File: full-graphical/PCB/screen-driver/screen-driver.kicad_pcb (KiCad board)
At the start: 2 copper layers, 139 x 139 mm, 159 parts, among them J1 Barrel_Jack_Switch, Q1 MPSA42, Q10 MPSA42, Q11 MPSA42, Q12 MPSA42, Q13 MPSA42, Q14 MPSA42, Q15 MPSA42, Q16 MPSA42, Q17 MPSA42, Q18 MPSA42, Q19 MPSA42, Q2 MPSA42, Q20 MPSA42, Q21 MPSA42, Q22 MPSA42, Q23 MPSA42, Q24 MPSA42, Q25 MPSA42, Q26 MPSA42, Q27 MPSA42, Q28 MPSA42, Q29 MPSA42, Q3 MPSA42, Q30 MPSA42, Q31 MPSA42, Q32 MPSA42, Q4 MPSA42, Q5 MPSA42, Q6 MPSA42, Q7 MPSA42, Q8 MPSA42, Q9 MPSA42, U1 SN755870, U2 ESP32-DEVKIT-V1, U3 SN755870, U4 TSR_1-2450, U5 CD4017BE, U6 CD4017BE

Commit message: first draft of full pcb
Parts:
- removed R117, R118, R119, R120, R121, R122, R123, R124, R125, R126: R, Resistor_THT:R_Axial_DIN0207_L6.3mm_D2.5mm_P7.62mm_Horizontal
- added C1: C_Small, Capacitor_THT:C_Disc_D3.8mm_W2.6mm_P2.50mm, F.Cu at (164.8, 72.6)
- added C2: C_Small, Capacitor_THT:C_Disc_D3.8mm_W2.6mm_P2.50mm, F.Cu at (212.3, 91.9)
- added C3: C_Small, Capacitor_THT:C_Disc_D3.8mm_W2.6mm_P2.50mm, F.Cu at (193.9, 63.3)
- added C4: C_Small, Capacitor_THT:C_Disc_D3.8mm_W2.6mm_P2.50mm, F.Cu at (145.6, 88.3)
- added J10: Conn_01x05_Male, Connector_PinHeader_2.54mm:PinHeader_1x05_P2.54mm_Vertical, B.Cu at (158.2, 83.3)
- added J2: ANODE - EVEN 2-60, Connector_PinHeader_2.00mm:PinHeader_1x40_P2.00mm_Vertical, F.Cu at (91.3, 33.2)
- added J3: ANODE - EVEN-62-100, Connector_PinHeader_2.00mm:PinHeader_1x20_P2.00mm_Vertical, F.Cu at (91.3, 113.2)
- added J4: CATHODE - EVEN - 42-100, Connector_PinHeader_2.00mm:PinHeader_1x40_P2.00mm_Vertical, F.Cu at (104.9, 28.1)
- added J5: CATHODE ODD 41-99, Connector_PinHeader_2.00mm:PinHeader_1x40_P2.00mm_Vertical, F.Cu at (104.7, 157.2)
- added J6: CATHODE EVEN 2-40, Connector_PinHeader_2.00mm:PinHeader_1x12_P2.00mm_Vertical, F.Cu at (184.9, 28.1)
- added J7: CATHODE ODD 1-39, Connector_PinHeader_2.00mm:PinHeader_1x12_P2.00mm_Vertical, F.Cu at (184.7, 157.2)
- added J8: ANODE - ODD 1-59, Connector_PinHeader_2.00mm:PinHeader_1x40_P2.00mm_Vertical, F.Cu at (220.3, 33.2)
- added J9: ANODE - ODD 61-99, Connector_PinHeader_2.00mm:PinHeader_1x20_P2.00mm_Vertical, F.Cu at (220.3, 113.2)
- added R111: R, Resistor_SMD:R_0201_0603Metric_Pad0.64x0.40mm_HandSolder, F.Cu at (217.0, 143.2)
- added R112: R, Resistor_THT:R_Axial_DIN0207_L6.3mm_D2.5mm_P7.62mm_Horizontal, F.Cu at (186.4, 45.8)
- added R113: R, Resistor_THT:R_Axial_DIN0207_L6.3mm_D2.5mm_P7.62mm_Horizontal, F.Cu at (158.4, 88.4)
- J1, U4: moved to B.Cu
- R102, R103, R104, R105, R106, R107, R108, R109, R110: footprint Resistor_THT:R_Axial_DIN0207_L6.3mm_D2.5mm_P7.62mm_Horizontal -> Resistor_SMD:R_0201_0603Metric_Pad0.64x0.40mm_HandSolder
- R51, R52, R53, R54, R55, R56, R57, R58, R59, R60: footprint Resistor_SMD:R_0201_0603Metric_Pad0.64x0.40mm_HandSolder -> Resistor_THT:R_Axial_DIN0207_L6.3mm_D2.5mm_P7.62mm_Horizontal
- U2: footprint ESP32-DEVKIT-V1:MODULE_ESP32_DEVKIT_V1 -> ESP32-DEVKITC-32D:MODULE_ESP32-DEVKITC-32D; moved to B.Cu
- U5, U6: footprint CD4017BE:DIP794W45P254L1969H508Q16 -> Package_DIP:DIP-16_W7.62mm
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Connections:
- J1 pad 1: unconnected-(J1-Pad1) -> Net-(J1-Pad1)
- J1 pad 2: unconnected-(J1-Pad2) -> GND
- Q1 pad 1: unconnected-(Q1-Pad1) -> GND
- Q1 pad 2: unconnected-(Q1-Pad2) -> Net-(Q1-Pad2)
- Q1 pad 3: unconnected-(Q1-Pad3) -> Net-(J3-Pad20)
- Q10 pad 1: unconnected-(Q10-Pad1) -> GND
- Q10 pad 2: unconnected-(Q10-Pad2) -> Net-(Q10-Pad2)
- Q10 pad 3: unconnected-(Q10-Pad3) -> Net-(J3-Pad17)
- Q11 pad 1: unconnected-(Q11-Pad1) -> Net-(Q11-Pad1)
- Q11 pad 2: unconnected-(Q11-Pad2) -> Net-(Q1-Pad2)
- Q11 pad 3: unconnected-(Q11-Pad3) -> Net-(J7-Pad11)
- Q12 pad 1: unconnected-(Q12-Pad1) -> Net-(Q11-Pad1)
- Q12 pad 2: unconnected-(Q12-Pad2) -> Net-(Q12-Pad2)
- Q12 pad 3: unconnected-(Q12-Pad3) -> Net-(J6-Pad11)
- Q13 pad 1: unconnected-(Q13-Pad1) -> Net-(Q11-Pad1)
- Q13 pad 2: unconnected-(Q13-Pad2) -> Net-(Q13-Pad2)
- Q13 pad 3: unconnected-(Q13-Pad3) -> Net-(J6-Pad8)
- Q14 pad 1: unconnected-(Q14-Pad1) -> Net-(Q11-Pad1)
- Q14 pad 2: unconnected-(Q14-Pad2) -> Net-(Q14-Pad2)
- Q14 pad 3: unconnected-(Q14-Pad3) -> Net-(J6-Pad5)
- Q15 pad 1: unconnected-(Q15-Pad1) -> Net-(Q11-Pad1)
- Q15 pad 2: unconnected-(Q15-Pad2) -> Net-(Q15-Pad2)
- Q15 pad 3: unconnected-(Q15-Pad3) -> Net-(J6-Pad2)
- Q16 pad 1: unconnected-(Q16-Pad1) -> Net-(Q11-Pad1)
- Q16 pad 2: unconnected-(Q16-Pad2) -> Net-(Q10-Pad2)
- Q16 pad 3: unconnected-(Q16-Pad3) -> Net-(J4-Pad39)
- Q17 pad 1: unconnected-(Q17-Pad1) -> Net-(Q11-Pad1)
- Q17 pad 2: unconnected-(Q17-Pad2) -> Net-(Q17-Pad2)
- Q17 pad 3: unconnected-(Q17-Pad3) -> Net-(J4-Pad36)
- Q18 pad 1: unconnected-(Q18-Pad1) -> Net-(Q11-Pad1)
- Q18 pad 2: unconnected-(Q18-Pad2) -> Net-(Q18-Pad2)
- Q18 pad 3: unconnected-(Q18-Pad3) -> Net-(J4-Pad33)
- Q19 pad 1: unconnected-(Q19-Pad1) -> Net-(Q11-Pad1)
- Q19 pad 2: unconnected-(Q19-Pad2) -> Net-(Q19-Pad2)
- Q19 pad 3: unconnected-(Q19-Pad3) -> Net-(J4-Pad30)
- Q2 pad 1: unconnected-(Q2-Pad1) -> GND
- Q2 pad 2: unconnected-(Q2-Pad2) -> Net-(Q12-Pad2)
- Q2 pad 3: unconnected-(Q2-Pad3) -> Net-(J2-Pad4)
- Q20 pad 1: unconnected-(Q20-Pad1) -> Net-(Q11-Pad1)
- Q20 pad 2: unconnected-(Q20-Pad2) -> Net-(Q20-Pad2)
- Q20 pad 3: unconnected-(Q20-Pad3) -> Net-(J4-Pad27)
- Q21 pad 1: unconnected-(Q21-Pad1) -> GND
- Q21 pad 2: unconnected-(Q21-Pad2) -> Net-(Q21-Pad2)
- Q21 pad 3: unconnected-(Q21-Pad3) -> Net-(Q11-Pad1)
- Q22 pad 1: unconnected-(Q22-Pad1) -> Net-(Q22-Pad1)
- Q22 pad 2: unconnected-(Q22-Pad2) -> Net-(Q1-Pad2)
- Q22 pad 3: unconnected-(Q22-Pad3) -> Net-(J4-Pad24)
- Q23 pad 1: unconnected-(Q23-Pad1) -> Net-(Q22-Pad1)
- Q23 pad 2: unconnected-(Q23-Pad2) -> Net-(Q12-Pad2)
- Q23 pad 3: unconnected-(Q23-Pad3) -> Net-(J4-Pad21)
- Q24 pad 1: unconnected-(Q24-Pad1) -> Net-(Q22-Pad1)
- Q24 pad 2: unconnected-(Q24-Pad2) -> Net-(Q13-Pad2)
- Q24 pad 3: unconnected-(Q24-Pad3) -> Net-(J4-Pad18)
- Q25 pad 1: unconnected-(Q25-Pad1) -> Net-(Q22-Pad1)
- Q25 pad 2: unconnected-(Q25-Pad2) -> Net-(Q14-Pad2)
- Q25 pad 3: unconnected-(Q25-Pad3) -> Net-(J4-Pad15)
- Q26 pad 1: unconnected-(Q26-Pad1) -> Net-(Q22-Pad1)
- Q26 pad 2: unconnected-(Q26-Pad2) -> Net-(Q15-Pad2)
- Q26 pad 3: unconnected-(Q26-Pad3) -> Net-(J4-Pad12)
- Q27 pad 1: unconnected-(Q27-Pad1) -> Net-(Q22-Pad1)
- Q27 pad 2: unconnected-(Q27-Pad2) -> Net-(Q10-Pad2)
- Q27 pad 3: unconnected-(Q27-Pad3) -> Net-(J4-Pad9)
- Q28 pad 1: unconnected-(Q28-Pad1) -> Net-(Q22-Pad1)
- Q28 pad 2: unconnected-(Q28-Pad2) -> Net-(Q17-Pad2)
- Q28 pad 3: unconnected-(Q28-Pad3) -> Net-(J4-Pad6)
- Q29 pad 1: unconnected-(Q29-Pad1) -> Net-(Q22-Pad1)
- Q29 pad 2: unconnected-(Q29-Pad2) -> Net-(Q18-Pad2)
- Q29 pad 3: unconnected-(Q29-Pad3) -> Net-(J4-Pad3)
- Q3 pad 1: unconnected-(Q3-Pad1) -> GND
- Q3 pad 2: unconnected-(Q3-Pad2) -> Net-(Q13-Pad2)
- Q3 pad 3: unconnected-(Q3-Pad3) -> Net-(J3-Pad18)
- Q30 pad 1: unconnected-(Q30-Pad1) -> Net-(Q22-Pad1)
- Q30 pad 2: unconnected-(Q30-Pad2) -> Net-(Q19-Pad2)
- Q30 pad 3: unconnected-(Q30-Pad3) -> Net-(J5-Pad1)
- Q31 pad 1: unconnected-(Q31-Pad1) -> Net-(Q22-Pad1)
- Q31 pad 2: unconnected-(Q31-Pad2) -> Net-(Q20-Pad2)
- Q31 pad 3: unconnected-(Q31-Pad3) -> Net-(J4-Pad2)
- Q32 pad 1: unconnected-(Q32-Pad1) -> GND
- Q32 pad 2: unconnected-(Q32-Pad2) -> Net-(Q32-Pad2)
- Q32 pad 3: unconnected-(Q32-Pad3) -> Net-(Q22-Pad1)
- Q4 pad 1: unconnected-(Q4-Pad1) -> GND
- Q4 pad 2: unconnected-(Q4-Pad2) -> Net-(Q20-Pad2)
- Q4 pad 3: unconnected-(Q4-Pad3) -> Net-(J2-Pad30)
- Q5 pad 1: unconnected-(Q5-Pad1) -> GND
- Q5 pad 2: unconnected-(Q5-Pad2) -> Net-(Q14-Pad2)
- Q5 pad 3: unconnected-(Q5-Pad3) -> Net-(J2-Pad1)
- Q6 pad 1: unconnected-(Q6-Pad1) -> GND
- Q6 pad 2: unconnected-(Q6-Pad2) -> Net-(Q19-Pad2)
- Q6 pad 3: unconnected-(Q6-Pad3) -> Net-(J2-Pad2)
- Q7 pad 1: unconnected-(Q7-Pad1) -> GND
- Q7 pad 2: unconnected-(Q7-Pad2) -> Net-(Q15-Pad2)
- Q7 pad 3: unconnected-(Q7-Pad3) -> Net-(J3-Pad19)
- Q8 pad 1: unconnected-(Q8-Pad1) -> GND
- Q8 pad 2: unconnected-(Q8-Pad2) -> Net-(Q18-Pad2)
- Q8 pad 3: unconnected-(Q8-Pad3) -> Net-(J2-Pad31)
- Q9 pad 1: unconnected-(Q9-Pad1) -> GND
- Q9 pad 2: unconnected-(Q9-Pad2) -> Net-(Q17-Pad2)
- Q9 pad 3: unconnected-(Q9-Pad3) -> Net-(J2-Pad3)
- R1 pad 1: unconnected-(R1-Pad1) -> Net-(J2-Pad5)
- R1 pad 2: unconnected-(R1-Pad2) -> Net-(R1-Pad2)
- R10 pad 1: unconnected-(R10-Pad1) -> Net-(J2-Pad14)
- R10 pad 2: unconnected-(R10-Pad2) -> Net-(R10-Pad2)
- R100 pad 1: unconnected-(R100-Pad1) -> Net-(J9-Pad6)
- R100 pad 2: unconnected-(R100-Pad2) -> Net-(R100-Pad2)
- R101 pad 1: unconnected-(R101-Pad1) -> Net-(R101-Pad1)
- R101 pad 2: unconnected-(R101-Pad2) -> Net-(Q20-Pad2)
- R102 pad 1: unconnected-(R102-Pad1) -> Net-(J9-Pad7)
- R102 pad 2: unconnected-(R102-Pad2) -> Net-(R102-Pad2)
- R103 pad 1: unconnected-(R103-Pad1) -> Net-(J9-Pad8)
- R103 pad 2: unconnected-(R103-Pad2) -> Net-(R103-Pad2)
- R104 pad 1: unconnected-(R104-Pad1) -> Net-(J9-Pad9)
- R104 pad 2: unconnected-(R104-Pad2) -> Net-(R104-Pad2)
- R105 pad 1: unconnected-(R105-Pad1) -> Net-(J9-Pad10)
- R105 pad 2: unconnected-(R105-Pad2) -> Net-(R105-Pad2)
- R106 pad 1: unconnected-(R106-Pad1) -> Net-(J9-Pad11)
- R106 pad 2: unconnected-(R106-Pad2) -> Net-(R106-Pad2)
- R107 pad 1: unconnected-(R107-Pad1) -> Net-(J9-Pad12)
- R107 pad 2: unconnected-(R107-Pad2) -> Net-(R107-Pad2)
- R108 pad 1: unconnected-(R108-Pad1) -> Net-(J9-Pad13)
- R108 pad 2: unconnected-(R108-Pad2) -> Net-(R108-Pad2)
- R109 pad 1: unconnected-(R109-Pad1) -> Net-(J9-Pad14)
- R109 pad 2: unconnected-(R109-Pad2) -> Net-(R109-Pad2)
- R11 pad 1: unconnected-(R11-Pad1) -> Net-(J2-Pad15)
- R11 pad 2: unconnected-(R11-Pad2) -> Net-(R11-Pad2)
- R110 pad 1: unconnected-(R110-Pad1) -> Net-(J9-Pad15)
- R110 pad 2: unconnected-(R110-Pad2) -> Net-(R110-Pad2)
- R12 pad 1: unconnected-(R12-Pad1) -> Net-(J2-Pad16)
- R12 pad 2: unconnected-(R12-Pad2) -> Net-(R12-Pad2)
- R13 pad 1: unconnected-(R13-Pad1) -> Net-(J2-Pad17)
- R13 pad 2: unconnected-(R13-Pad2) -> Net-(R13-Pad2)
- R14 pad 1: unconnected-(R14-Pad1) -> Net-(J2-Pad18)
- R14 pad 2: unconnected-(R14-Pad2) -> Net-(R14-Pad2)
- R15 pad 1: unconnected-(R15-Pad1) -> Net-(J2-Pad19)
- R15 pad 2: unconnected-(R15-Pad2) -> Net-(R15-Pad2)
- R16 pad 1: unconnected-(R16-Pad1) -> Net-(J2-Pad20)
- R16 pad 2: unconnected-(R16-Pad2) -> Net-(R16-Pad2)
- R17 pad 1: unconnected-(R17-Pad1) -> Net-(J2-Pad21)
- R17 pad 2: unconnected-(R17-Pad2) -> Net-(R17-Pad2)
- R18 pad 1: unconnected-(R18-Pad1) -> Net-(J2-Pad22)
- R18 pad 2: unconnected-(R18-Pad2) -> Net-(R18-Pad2)
- R19 pad 1: unconnected-(R19-Pad1) -> Net-(J2-Pad23)
- R19 pad 2: unconnected-(R19-Pad2) -> Net-(R19-Pad2)
- R2 pad 1: unconnected-(R2-Pad1) -> Net-(J2-Pad6)
- R2 pad 2: unconnected-(R2-Pad2) -> Net-(R2-Pad2)
- R20 pad 1: unconnected-(R20-Pad1) -> Net-(J2-Pad24)
- R20 pad 2: unconnected-(R20-Pad2) -> Net-(R20-Pad2)
- R21 pad 1: unconnected-(R21-Pad1) -> Net-(J2-Pad25)
- R21 pad 2: unconnected-(R21-Pad2) -> Net-(R21-Pad2)
- R22 pad 1: unconnected-(R22-Pad1) -> Net-(J2-Pad26)
- R22 pad 2: unconnected-(R22-Pad2) -> Net-(R22-Pad2)
- R23 pad 1: unconnected-(R23-Pad1) -> Net-(J2-Pad27)
- R23 pad 2: unconnected-(R23-Pad2) -> Net-(R23-Pad2)
- R24 pad 1: unconnected-(R24-Pad1) -> Net-(J2-Pad28)
- R24 pad 2: unconnected-(R24-Pad2) -> Net-(R24-Pad2)
- R25 pad 1: unconnected-(R25-Pad1) -> Net-(J2-Pad29)
- R25 pad 2: unconnected-(R25-Pad2) -> Net-(R25-Pad2)
- R26 pad 1: unconnected-(R26-Pad1) -> Net-(J2-Pad32)
- R26 pad 2: unconnected-(R26-Pad2) -> Net-(R26-Pad2)
- R27 pad 1: unconnected-(R27-Pad1) -> Net-(J2-Pad33)
- R27 pad 2: unconnected-(R27-Pad2) -> Net-(R27-Pad2)
- R28 pad 1: unconnected-(R28-Pad1) -> Net-(J2-Pad34)
- R28 pad 2: unconnected-(R28-Pad2) -> Net-(R28-Pad2)
- R29 pad 1: unconnected-(R29-Pad1) -> Net-(J2-Pad35)
- R29 pad 2: unconnected-(R29-Pad2) -> Net-(R29-Pad2)
- R3 pad 1: unconnected-(R3-Pad1) -> Net-(J2-Pad7)
- R3 pad 2: unconnected-(R3-Pad2) -> Net-(R3-Pad2)
- R30 pad 1: unconnected-(R30-Pad1) -> Net-(J2-Pad36)
- R30 pad 2: unconnected-(R30-Pad2) -> Net-(R30-Pad2)
- R31 pad 1: unconnected-(R31-Pad1) -> Net-(J2-Pad37)
- R31 pad 2: unconnected-(R31-Pad2) -> Net-(R31-Pad2)
- R32 pad 1: unconnected-(R32-Pad1) -> Net-(J2-Pad38)
- R32 pad 2: unconnected-(R32-Pad2) -> Net-(R32-Pad2)
- R33 pad 1: unconnected-(R33-Pad1) -> Net-(J2-Pad39)
- R33 pad 2: unconnected-(R33-Pad2) -> Net-(R33-Pad2)
- R34 pad 1: unconnected-(R34-Pad1) -> Net-(J2-Pad40)
- R34 pad 2: unconnected-(R34-Pad2) -> Net-(R34-Pad2)
- R35 pad 1: unconnected-(R35-Pad1) -> Net-(J3-Pad1)
- R35 pad 2: unconnected-(R35-Pad2) -> Net-(R35-Pad2)
- R36 pad 1: unconnected-(R36-Pad1) -> Net-(J3-Pad2)
- R36 pad 2: unconnected-(R36-Pad2) -> Net-(R36-Pad2)
- R37 pad 1: unconnected-(R37-Pad1) -> Net-(J3-Pad3)
- R37 pad 2: unconnected-(R37-Pad2) -> Net-(R37-Pad2)
- R38 pad 1: unconnected-(R38-Pad1) -> Net-(J3-Pad4)
- R38 pad 2: unconnected-(R38-Pad2) -> Net-(R38-Pad2)
- R39 pad 1: unconnected-(R39-Pad1) -> Net-(J3-Pad5)
- R39 pad 2: unconnected-(R39-Pad2) -> Net-(R39-Pad2)
- R4 pad 1: unconnected-(R4-Pad1) -> Net-(J2-Pad8)
- R4 pad 2: unconnected-(R4-Pad2) -> Net-(R4-Pad2)
- R40 pad 1: unconnected-(R40-Pad1) -> Net-(J3-Pad6)
- R40 pad 2: unconnected-(R40-Pad2) -> Net-(R40-Pad2)
- R41 pad 1: unconnected-(R41-Pad1) -> Net-(J3-Pad7)
- R41 pad 2: unconnected-(R41-Pad2) -> Net-(R41-Pad2)
- R42 pad 1: unconnected-(R42-Pad1) -> Net-(J3-Pad8)
- R42 pad 2: unconnected-(R42-Pad2) -> Net-(R42-Pad2)
- R43 pad 1: unconnected-(R43-Pad1) -> Net-(J3-Pad9)
- R43 pad 2: unconnected-(R43-Pad2) -> Net-(R43-Pad2)
- R44 pad 1: unconnected-(R44-Pad1) -> Net-(J3-Pad10)
- R44 pad 2: unconnected-(R44-Pad2) -> Net-(R44-Pad2)
- R45 pad 1: unconnected-(R45-Pad1) -> Net-(J3-Pad11)
- R45 pad 2: unconnected-(R45-Pad2) -> Net-(R45-Pad2)
- R46 pad 1: unconnected-(R46-Pad1) -> Net-(J3-Pad12)
- R46 pad 2: unconnected-(R46-Pad2) -> Net-(R46-Pad2)
- R47 pad 1: unconnected-(R47-Pad1) -> Net-(J3-Pad13)
- R47 pad 2: unconnected-(R47-Pad2) -> Net-(R47-Pad2)
- R48 pad 1: unconnected-(R48-Pad1) -> Net-(J3-Pad14)
- R48 pad 2: unconnected-(R48-Pad2) -> Net-(R48-Pad2)
- R49 pad 1: unconnected-(R49-Pad1) -> Net-(J3-Pad15)
- R49 pad 2: unconnected-(R49-Pad2) -> Net-(R49-Pad2)
- R5 pad 1: unconnected-(R5-Pad1) -> Net-(J2-Pad9)
- R5 pad 2: unconnected-(R5-Pad2) -> Net-(R5-Pad2)
- R50 pad 1: unconnected-(R50-Pad1) -> Net-(J3-Pad16)
- R50 pad 2: unconnected-(R50-Pad2) -> Net-(R50-Pad2)
- R51 pad 1: unconnected-(R51-Pad1) -> Net-(R51-Pad1)
- R51 pad 2: unconnected-(R51-Pad2) -> Net-(Q18-Pad2)
- R52 pad 1: unconnected-(R52-Pad1) -> Net-(R52-Pad1)
- R52 pad 2: unconnected-(R52-Pad2) -> Net-(Q17-Pad2)
- R53 pad 1: unconnected-(R53-Pad1) -> Net-(R53-Pad1)
- R53 pad 2: unconnected-(R53-Pad2) -> Net-(Q10-Pad2)
- R54 pad 1: unconnected-(R54-Pad1) -> Net-(R54-Pad1)
- R54 pad 2: unconnected-(R54-Pad2) -> Net-(Q15-Pad2)
- R55 pad 1: unconnected-(R55-Pad1) -> Net-(R55-Pad1)
- R55 pad 2: unconnected-(R55-Pad2) -> Net-(Q19-Pad2)
- R56 pad 1: unconnected-(R56-Pad1) -> Net-(R56-Pad1)
- R56 pad 2: unconnected-(R56-Pad2) -> Net-(Q14-Pad2)
- R57 pad 1: unconnected-(R57-Pad1) -> Net-(R57-Pad1)
- R57 pad 2: unconnected-(R57-Pad2) -> Net-(Q13-Pad2)
- R58 pad 1: unconnected-(R58-Pad1) -> Net-(R58-Pad1)
- R58 pad 2: unconnected-(R58-Pad2) -> Net-(Q12-Pad2)
- R59 pad 1: unconnected-(R59-Pad1) -> Net-(R59-Pad1)
- R59 pad 2: unconnected-(R59-Pad2) -> Net-(Q1-Pad2)
- R6 pad 1: unconnected-(R6-Pad1) -> Net-(J2-Pad10)
- R6 pad 2: unconnected-(R6-Pad2) -> Net-(R6-Pad2)
- R60 pad 1: unconnected-(R60-Pad1) -> Net-(R60-Pad1)
- R60 pad 2: unconnected-(R60-Pad2) -> Net-(Q21-Pad2)
- R61 pad 1: unconnected-(R61-Pad1) -> Net-(J8-Pad5)
- R61 pad 2: unconnected-(R61-Pad2) -> Net-(R61-Pad2)
- R62 pad 1: unconnected-(R62-Pad1) -> Net-(J8-Pad6)
- R62 pad 2: unconnected-(R62-Pad2) -> Net-(R62-Pad2)
- R63 pad 1: unconnected-(R63-Pad1) -> Net-(J8-Pad7)
- R63 pad 2: unconnected-(R63-Pad2) -> Net-(R63-Pad2)
- R64 pad 1: unconnected-(R64-Pad1) -> Net-(J8-Pad8)
- R64 pad 2: unconnected-(R64-Pad2) -> Net-(R64-Pad2)
- R65 pad 1: unconnected-(R65-Pad1) -> Net-(J8-Pad9)
- R65 pad 2: unconnected-(R65-Pad2) -> Net-(R65-Pad2)
- R66 pad 1: unconnected-(R66-Pad1) -> Net-(J8-Pad10)
- R66 pad 2: unconnected-(R66-Pad2) -> Net-(R66-Pad2)
- R67 pad 1: unconnected-(R67-Pad1) -> Net-(J8-Pad11)
- R67 pad 2: unconnected-(R67-Pad2) -> Net-(R67-Pad2)
- R68 pad 1: unconnected-(R68-Pad1) -> Net-(J8-Pad12)
- R68 pad 2: unconnected-(R68-Pad2) -> Net-(R68-Pad2)
- R69 pad 1: unconnected-(R69-Pad1) -> Net-(J8-Pad13)
- R69 pad 2: unconnected-(R69-Pad2) -> Net-(R69-Pad2)
- R7 pad 1: unconnected-(R7-Pad1) -> Net-(J2-Pad11)
- R7 pad 2: unconnected-(R7-Pad2) -> Net-(R7-Pad2)
- R70 pad 1: unconnected-(R70-Pad1) -> Net-(J8-Pad14)
- R70 pad 2: unconnected-(R70-Pad2) -> Net-(R70-Pad2)
- R71 pad 1: unconnected-(R71-Pad1) -> Net-(J8-Pad15)
- R71 pad 2: unconnected-(R71-Pad2) -> Net-(R71-Pad2)
- R72 pad 1: unconnected-(R72-Pad1) -> Net-(J8-Pad16)
- R72 pad 2: unconnected-(R72-Pad2) -> Net-(R72-Pad2)
- R73 pad 1: unconnected-(R73-Pad1) -> Net-(J8-Pad17)
- R73 pad 2: unconnected-(R73-Pad2) -> Net-(R73-Pad2)
- R74 pad 1: unconnected-(R74-Pad1) -> Net-(J8-Pad18)
- R74 pad 2: unconnected-(R74-Pad2) -> Net-(R74-Pad2)
- R75 pad 1: unconnected-(R75-Pad1) -> Net-(J8-Pad19)
- R75 pad 2: unconnected-(R75-Pad2) -> Net-(R75-Pad2)
- R76 pad 1: unconnected-(R76-Pad1) -> Net-(J8-Pad20)
- R76 pad 2: unconnected-(R76-Pad2) -> Net-(R76-Pad2)
- R77 pad 1: unconnected-(R77-Pad1) -> Net-(J8-Pad21)
- R77 pad 2: unconnected-(R77-Pad2) -> Net-(R77-Pad2)
- R78 pad 1: unconnected-(R78-Pad1) -> Net-(J8-Pad22)
- R78 pad 2: unconnected-(R78-Pad2) -> Net-(R78-Pad2)
- R79 pad 1: unconnected-(R79-Pad1) -> Net-(J8-Pad23)
- R79 pad 2: unconnected-(R79-Pad2) -> Net-(R79-Pad2)
- R8 pad 1: unconnected-(R8-Pad1) -> Net-(J2-Pad12)
- R8 pad 2: unconnected-(R8-Pad2) -> Net-(R8-Pad2)
- R80 pad 1: unconnected-(R80-Pad1) -> Net-(J8-Pad24)
- R80 pad 2: unconnected-(R80-Pad2) -> Net-(R80-Pad2)
- R81 pad 1: unconnected-(R81-Pad1) -> Net-(J8-Pad25)
- R81 pad 2: unconnected-(R81-Pad2) -> Net-(R81-Pad2)
- R82 pad 1: unconnected-(R82-Pad1) -> Net-(J8-Pad26)
- R82 pad 2: unconnected-(R82-Pad2) -> Net-(R82-Pad2)
- R83 pad 1: unconnected-(R83-Pad1) -> Net-(J8-Pad27)
- R83 pad 2: unconnected-(R83-Pad2) -> Net-(R83-Pad2)
- R84 pad 1: unconnected-(R84-Pad1) -> Net-(J8-Pad28)
- R84 pad 2: unconnected-(R84-Pad2) -> Net-(R84-Pad2)
- R85 pad 1: unconnected-(R85-Pad1) -> Net-(J8-Pad29)
- R85 pad 2: unconnected-(R85-Pad2) -> Net-(R85-Pad2)
- R86 pad 1: unconnected-(R86-Pad1) -> Net-(J8-Pad32)
- R86 pad 2: unconnected-(R86-Pad2) -> Net-(R86-Pad2)
- R87 pad 1: unconnected-(R87-Pad1) -> Net-(J8-Pad33)
- R87 pad 2: unconnected-(R87-Pad2) -> Net-(R87-Pad2)
- R88 pad 1: unconnected-(R88-Pad1) -> Net-(J8-Pad34)
- R88 pad 2: unconnected-(R88-Pad2) -> Net-(R88-Pad2)
- R89 pad 1: unconnected-(R89-Pad1) -> Net-(J8-Pad35)
- R89 pad 2: unconnected-(R89-Pad2) -> Net-(R89-Pad2)
- R9 pad 1: unconnected-(R9-Pad1) -> Net-(J2-Pad13)
- R9 pad 2: unconnected-(R9-Pad2) -> Net-(R9-Pad2)
- R90 pad 1: unconnected-(R90-Pad1) -> Net-(J8-Pad36)
- R90 pad 2: unconnected-(R90-Pad2) -> Net-(R90-Pad2)
- R91 pad 1: unconnected-(R91-Pad1) -> Net-(J8-Pad37)
- R91 pad 2: unconnected-(R91-Pad2) -> Net-(R91-Pad2)
- R92 pad 1: unconnected-(R92-Pad1) -> Net-(J8-Pad38)
- R92 pad 2: unconnected-(R92-Pad2) -> Net-(R92-Pad2)
- R93 pad 1: unconnected-(R93-Pad1) -> Net-(J8-Pad39)
- R93 pad 2: unconnected-(R93-Pad2) -> Net-(R93-Pad2)
- R94 pad 1: unconnected-(R94-Pad1) -> Net-(J8-Pad40)
- R94 pad 2: unconnected-(R94-Pad2) -> Net-(R94-Pad2)
- R95 pad 1: unconnected-(R95-Pad1) -> Net-(J9-Pad1)
- R95 pad 2: unconnected-(R95-Pad2) -> Net-(R95-Pad2)
- R96 pad 1: unconnected-(R96-Pad1) -> Net-(J9-Pad2)
- R96 pad 2: unconnected-(R96-Pad2) -> Net-(R96-Pad2)
- R97 pad 1: unconnected-(R97-Pad1) -> Net-(J9-Pad3)
- R97 pad 2: unconnected-(R97-Pad2) -> Net-(R97-Pad2)
- R98 pad 1: unconnected-(R98-Pad1) -> Net-(J9-Pad4)
- R98 pad 2: unconnected-(R98-Pad2) -> Net-(R98-Pad2)
- R99 pad 1: unconnected-(R99-Pad1) -> Net-(J9-Pad5)
- R99 pad 2: unconnected-(R99-Pad2) -> Net-(R99-Pad2)
- U1 pad 1: unconnected-(U1-Pad1) -> Net-(R3-Pad2)
- U1 pad 10: unconnected-(U1-Pad10) -> Net-(R12-Pad2)
- U1 pad 100: unconnected-(U1-Pad100) -> Net-(R2-Pad2)
- U1 pad 11: unconnected-(U1-Pad11) -> Net-(R13-Pad2)
- U1 pad 12: unconnected-(U1-Pad12) -> Net-(R14-Pad2)
- U1 pad 13: unconnected-(U1-Pad13) -> Net-(R15-Pad2)
- U1 pad 14: unconnected-(U1-Pad14) -> Net-(R16-Pad2)
- U1 pad 15: unconnected-(U1-Pad15) -> Net-(R17-Pad2)
- U1 pad 16: unconnected-(U1-Pad16) -> Net-(R18-Pad2)
- U1 pad 17: unconnected-(U1-Pad17) -> Net-(R19-Pad2)
- U1 pad 18: unconnected-(U1-Pad18) -> Net-(R20-Pad2)
- U1 pad 19: unconnected-(U1-Pad19) -> Net-(R21-Pad2)
- U1 pad 2: unconnected-(U1-Pad2) -> Net-(R4-Pad2)
- U1 pad 20: unconnected-(U1-Pad20) -> Net-(R22-Pad2)
- U1 pad 21: unconnected-(U1-Pad21) -> Net-(R23-Pad2)
- U1 pad 22: unconnected-(U1-Pad22) -> Net-(R24-Pad2)
- U1 pad 23: unconnected-(U1-Pad23) -> Net-(R25-Pad2)
- U1 pad 24: unconnected-(U1-Pad24) -> Net-(R26-Pad2)
- U1 pad 25: unconnected-(U1-Pad25) -> Net-(R27-Pad2)
- U1 pad 26: unconnected-(U1-Pad26) -> Net-(R28-Pad2)
- U1 pad 27: unconnected-(U1-Pad27) -> Net-(R29-Pad2)
- U1 pad 28: unconnected-(U1-Pad28) -> Net-(R30-Pad2)
- U1 pad 29: unconnected-(U1-Pad29) -> Net-(R31-Pad2)
- U1 pad 3: unconnected-(U1-Pad3) -> Net-(R5-Pad2)
- U1 pad 30: unconnected-(U1-Pad30) -> Net-(R32-Pad2)
- U1 pad 32: unconnected-(U1-Pad32) -> GND
- U1 pad 33: unconnected-(U1-Pad33) -> GND
- U1 pad 35: unconnected-(U1-Pad35) -> GND
- U1 pad 36: unconnected-(U1-Pad36) -> GND
- U1 pad 37: unconnected-(U1-Pad37) -> GND
- U1 pad 39: unconnected-(U1-Pad39) -> GND
- U1 pad 4: unconnected-(U1-Pad4) -> Net-(R6-Pad2)
- U1 pad 40: unconnected-(U1-Pad40) -> GND
- U1 pad 41: unconnected-(U1-Pad41) -> GND
- U1 pad 43: unconnected-(U1-Pad43) -> GND
- U1 pad 44: unconnected-(U1-Pad44) -> Net-(J10-Pad3)
- U1 pad 46: unconnected-(U1-Pad46) -> Net-(R33-Pad2)
- U1 pad 47: unconnected-(U1-Pad47) -> Net-(R34-Pad2)
- U1 pad 48: unconnected-(U1-Pad48) -> Net-(R35-Pad2)
- U1 pad 49: unconnected-(U1-Pad49) -> Net-(R36-Pad2)
- U1 pad 5: unconnected-(U1-Pad5) -> Net-(R7-Pad2)
- U1 pad 50: unconnected-(U1-Pad50) -> Net-(R37-Pad2)
- U1 pad 51: unconnected-(U1-Pad51) -> Net-(R38-Pad2)
- U1 pad 52: unconnected-(U1-Pad52) -> Net-(R39-Pad2)
- U1 pad 53: unconnected-(U1-Pad53) -> Net-(R40-Pad2)
- U1 pad 54: unconnected-(U1-Pad54) -> Net-(R41-Pad2)
- U1 pad 55: unconnected-(U1-Pad55) -> Net-(R42-Pad2)
- U1 pad 56: unconnected-(U1-Pad56) -> Net-(R43-Pad2)
- U1 pad 57: unconnected-(U1-Pad57) -> Net-(R44-Pad2)
- U1 pad 58: unconnected-(U1-Pad58) -> Net-(R45-Pad2)
- U1 pad 59: unconnected-(U1-Pad59) -> Net-(R46-Pad2)
- U1 pad 6: unconnected-(U1-Pad6) -> Net-(R8-Pad2)
- U1 pad 60: unconnected-(U1-Pad60) -> Net-(R47-Pad2)
- U1 pad 61: unconnected-(U1-Pad61) -> Net-(R48-Pad2)
- U1 pad 62: unconnected-(U1-Pad62) -> Net-(R49-Pad2)
- U1 pad 63: unconnected-(U1-Pad63) -> Net-(R50-Pad2)
- U1 pad 7: unconnected-(U1-Pad7) -> Net-(R9-Pad2)
- U1 pad 79: unconnected-(U1-Pad79) -> GND
- U1 pad 8: unconnected-(U1-Pad8) -> Net-(R10-Pad2)
- U1 pad 80: VDDH -> GND
- U1 pad 82: unconnected-(U1-Pad82) -> GND
- U1 pad 83: unconnected-(U1-Pad83) -> GND
- U1 pad 84: unconnected-(U1-Pad84) -> Net-(U1-Pad84)
- U1 pad 86: unconnected-(U1-Pad86) -> Net-(U1-Pad86)
- U1 pad 87: unconnected-(U1-Pad87) -> Net-(U1-Pad87)
- U1 pad 88: unconnected-(U1-Pad88) -> +3V3
- U1 pad 89: unconnected-(U1-Pad89) -> Net-(U1-Pad89)
- U1 pad 9: unconnected-(U1-Pad9) -> Net-(R11-Pad2)
- U1 pad 90: unconnected-(U1-Pad90) -> Net-(U1-Pad90)
- U1 pad 91: unconnected-(U1-Pad91) -> Net-(U1-Pad91)
- U1 pad 92: unconnected-(U1-Pad92) -> Net-(U1-Pad92)
- U1 pad 93: unconnected-(U1-Pad93) -> GND
- U1 pad 96: unconnected-(U1-Pad96) -> GND
- U1 pad 97: unconnected-(U1-Pad97) -> GND
- U1 pad 99: unconnected-(U1-Pad99) -> Net-(R1-Pad2)
- U2 pad 1: unconnected-(U2-Pad1) -> +3V3
- U2 pad 10: unconnected-(U2-Pad10) -> Net-(U2-Pad10)
- U2 pad 14: unconnected-(U2-Pad14) -> Net-(U2-Pad14)
- U2 pad 15: unconnected-(U2-Pad15) -> Net-(U2-Pad15)
- U2 pad 19: unconnected-(U2-Pad19) -> Net-(U2-Pad19)
- U2 pad 2: Net-(U2-Pad2) -> GND
- U2 pad 20: unconnected-(U2-Pad20) -> Net-(U2-Pad20)
- U2 pad 21: unconnected-(U2-Pad21) -> Net-(U2-Pad21)
- U2 pad 22: unconnected-(U2-Pad22) -> Net-(U2-Pad22)
- U2 pad 23: unconnected-(U2-Pad23) -> Net-(U2-Pad23)
- U2 pad 24: unconnected-(U2-Pad24) -> Net-(U2-Pad24)
- U2 pad 25: unconnected-(U2-Pad25) -> Net-(U2-Pad25)
- U2 pad 26: unconnected-(U2-Pad26) -> Net-(U1-Pad91)
- U2 pad 27: unconnected-(U2-Pad27) -> Net-(U1-Pad84)
- U2 pad 28: unconnected-(U2-Pad28) -> Net-(U1-Pad92)
- U2 pad 29: Net-(U2-Pad2) -> GND
- U2 pad 3: unconnected-(U2-Pad3) -> Net-(U1-Pad87)
- U2 pad 30: unconnected-(U2-Pad30) -> +5V
- U2 pad 4: unconnected-(U2-Pad4) -> Net-(U1-Pad86)
- U2 pad 5: unconnected-(U2-Pad5) -> Net-(U1-Pad89)
- U2 pad 8: unconnected-(U2-Pad8) -> Net-(U1-Pad90)
- U3 pad 1: unconnected-(U3-Pad1) -> Net-(R63-Pad2)
- U3 pad 10: unconnected-(U3-Pad10) -> Net-(R72-Pad2)
- U3 pad 100: unconnected-(U3-Pad100) -> Net-(R62-Pad2)
- U3 pad 11: unconnected-(U3-Pad11) -> Net-(R73-Pad2)
- U3 pad 12: unconnected-(U3-Pad12) -> Net-(R74-Pad2)
- U3 pad 13: unconnected-(U3-Pad13) -> Net-(R75-Pad2)
- U3 pad 14: unconnected-(U3-Pad14) -> Net-(R76-Pad2)
- U3 pad 15: unconnected-(U3-Pad15) -> Net-(R77-Pad2)
- U3 pad 16: unconnected-(U3-Pad16) -> Net-(R78-Pad2)
- U3 pad 17: unconnected-(U3-Pad17) -> Net-(R79-Pad2)
- U3 pad 18: unconnected-(U3-Pad18) -> Net-(R80-Pad2)
- U3 pad 19: unconnected-(U3-Pad19) -> Net-(R81-Pad2)
- U3 pad 2: unconnected-(U3-Pad2) -> Net-(R64-Pad2)
- U3 pad 20: unconnected-(U3-Pad20) -> Net-(R82-Pad2)
- U3 pad 21: unconnected-(U3-Pad21) -> Net-(R83-Pad2)
- U3 pad 22: unconnected-(U3-Pad22) -> Net-(R84-Pad2)
- U3 pad 23: unconnected-(U3-Pad23) -> Net-(R85-Pad2)
- U3 pad 24: unconnected-(U3-Pad24) -> Net-(R86-Pad2)
- U3 pad 25: unconnected-(U3-Pad25) -> Net-(R87-Pad2)
- U3 pad 26: unconnected-(U3-Pad26) -> Net-(R88-Pad2)
- U3 pad 27: unconnected-(U3-Pad27) -> Net-(R89-Pad2)
- U3 pad 28: unconnected-(U3-Pad28) -> Net-(R90-Pad2)
- U3 pad 29: unconnected-(U3-Pad29) -> Net-(R91-Pad2)
- U3 pad 3: unconnected-(U3-Pad3) -> Net-(R65-Pad2)
- U3 pad 30: unconnected-(U3-Pad30) -> Net-(R92-Pad2)
- U3 pad 32: unconnected-(U3-Pad32) -> Net-(J10-Pad3)
- U3 pad 33: unconnected-(U3-Pad33) -> Net-(J10-Pad3)
- U3 pad 35: unconnected-(U3-Pad35) -> GND
- U3 pad 36: unconnected-(U3-Pad36) -> GND
- U3 pad 37: unconnected-(U3-Pad37) -> GND
- U3 pad 39: unconnected-(U3-Pad39) -> GND
- U3 pad 4: unconnected-(U3-Pad4) -> Net-(R66-Pad2)
- U3 pad 40: unconnected-(U3-Pad40) -> GND
- U3 pad 41: unconnected-(U3-Pad41) -> GND
- U3 pad 43: unconnected-(U3-Pad43) -> Net-(J10-Pad3)
- U3 pad 44: unconnected-(U3-Pad44) -> Net-(J10-Pad3)
- U3 pad 46: unconnected-(U3-Pad46) -> Net-(R93-Pad2)
- U3 pad 47: unconnected-(U3-Pad47) -> Net-(R94-Pad2)
- U3 pad 48: unconnected-(U3-Pad48) -> Net-(R95-Pad2)
- U3 pad 49: unconnected-(U3-Pad49) -> Net-(R96-Pad2)
- U3 pad 5: unconnected-(U3-Pad5) -> Net-(R67-Pad2)
- U3 pad 50: unconnected-(U3-Pad50) -> Net-(R97-Pad2)
- U3 pad 51: unconnected-(U3-Pad51) -> Net-(R98-Pad2)
- U3 pad 52: unconnected-(U3-Pad52) -> Net-(R99-Pad2)
- U3 pad 53: unconnected-(U3-Pad53) -> Net-(R100-Pad2)
- U3 pad 54: unconnected-(U3-Pad54) -> Net-(R102-Pad2)
- U3 pad 55: unconnected-(U3-Pad55) -> Net-(R103-Pad2)
- U3 pad 56: unconnected-(U3-Pad56) -> Net-(R104-Pad2)
- U3 pad 57: unconnected-(U3-Pad57) -> Net-(R105-Pad2)
- U3 pad 58: unconnected-(U3-Pad58) -> Net-(R106-Pad2)
- U3 pad 59: unconnected-(U3-Pad59) -> Net-(R107-Pad2)
- U3 pad 6: unconnected-(U3-Pad6) -> Net-(R68-Pad2)
- U3 pad 60: unconnected-(U3-Pad60) -> Net-(R108-Pad2)
- U3 pad 61: unconnected-(U3-Pad61) -> Net-(R109-Pad2)
- U3 pad 62: unconnected-(U3-Pad62) -> Net-(R110-Pad2)
- U3 pad 63: unconnected-(U3-Pad63) -> Net-(R111-Pad2)
- U3 pad 7: unconnected-(U3-Pad7) -> Net-(R69-Pad2)
- U3 pad 79: unconnected-(U3-Pad79) -> Net-(J10-Pad3)
- U3 pad 8: unconnected-(U3-Pad8) -> Net-(R70-Pad2)
- U3 pad 80: VDDH -> Net-(J10-Pad3)
- U3 pad 82: unconnected-(U3-Pad82) -> GND
- U3 pad 83: unconnected-(U3-Pad83) -> GND
- U3 pad 84: unconnected-(U3-Pad84) -> Net-(U2-Pad24)
- U3 pad 86: unconnected-(U3-Pad86) -> Net-(U2-Pad22)
- U3 pad 87: unconnected-(U3-Pad87) -> Net-(U2-Pad14)
- U3 pad 88: unconnected-(U3-Pad88) -> +3V3
- U3 pad 89: unconnected-(U3-Pad89) -> Net-(U2-Pad21)
- U3 pad 9: unconnected-(U3-Pad9) -> Net-(R71-Pad2)
- U3 pad 90: unconnected-(U3-Pad90) -> Net-(U2-Pad25)
- U3 pad 91: unconnected-(U3-Pad91) -> Net-(U2-Pad15)
- U3 pad 92: unconnected-(U3-Pad92) -> Net-(U2-Pad23)
- U3 pad 93: unconnected-(U3-Pad93) -> GND
- U3 pad 94: unconnected-(U3-Pad94) -> GND
- U3 pad 96: unconnected-(U3-Pad96) -> Net-(J10-Pad3)
- U3 pad 97: unconnected-(U3-Pad97) -> Net-(J10-Pad3)
- U3 pad 99: unconnected-(U3-Pad99) -> Net-(R61-Pad2)
- U4 pad 1: unconnected-(U4-Pad1) -> Net-(J1-Pad1)
- U4 pad 2: unconnected-(U4-Pad2) -> GND
- U4 pad 3: unconnected-(U4-Pad3) -> +5V
- U5 pad 1: unconnected-(U5-Pad1) -> Net-(R54-Pad1)
- U5 pad 10: unconnected-(U5-Pad10) -> Net-(R53-Pad1)
- U5 pad 11: unconnected-(U5-Pad11) -> Net-(R59-Pad1)
- U5 pad 15: unconnected-(U5-Pad15) -> Net-(U2-Pad10)
- U5 pad 16: unconnected-(U5-Pad16) -> +3V3
- U5 pad 2: unconnected-(U5-Pad2) -> Net-(R55-Pad1)
- U5 pad 3: unconnected-(U5-Pad3) -> Net-(R101-Pad1)
- U5 pad 4: unconnected-(U5-Pad4) -> Net-(R51-Pad1)
- U5 pad 5: unconnected-(U5-Pad5) -> Net-(R56-Pad1)
- U5 pad 6: unconnected-(U5-Pad6) -> Net-(R57-Pad1)
- U5 pad 7: unconnected-(U5-Pad7) -> Net-(R52-Pad1)
- U5 pad 8: unconnected-(U5-Pad8) -> GND
- U5 pad 9: unconnected-(U5-Pad9) -> Net-(R58-Pad1)
- U6 pad 1: unconnected-(U6-Pad1) -> Net-(J9-Pad20)
- U6 pad 10: unconnected-(U6-Pad10) -> Net-(J8-Pad2)
- U6 pad 11: unconnected-(U6-Pad11) -> Net-(R112-Pad1)
- U6 pad 14: unconnected-(U6-Pad14) -> Net-(U2-Pad19)
- U6 pad 15: unconnected-(U6-Pad15) -> Net-(U2-Pad20)
- U6 pad 16: unconnected-(U6-Pad16) -> +3V3
- U6 pad 2: unconnected-(U6-Pad2) -> Net-(J9-Pad18)
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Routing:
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
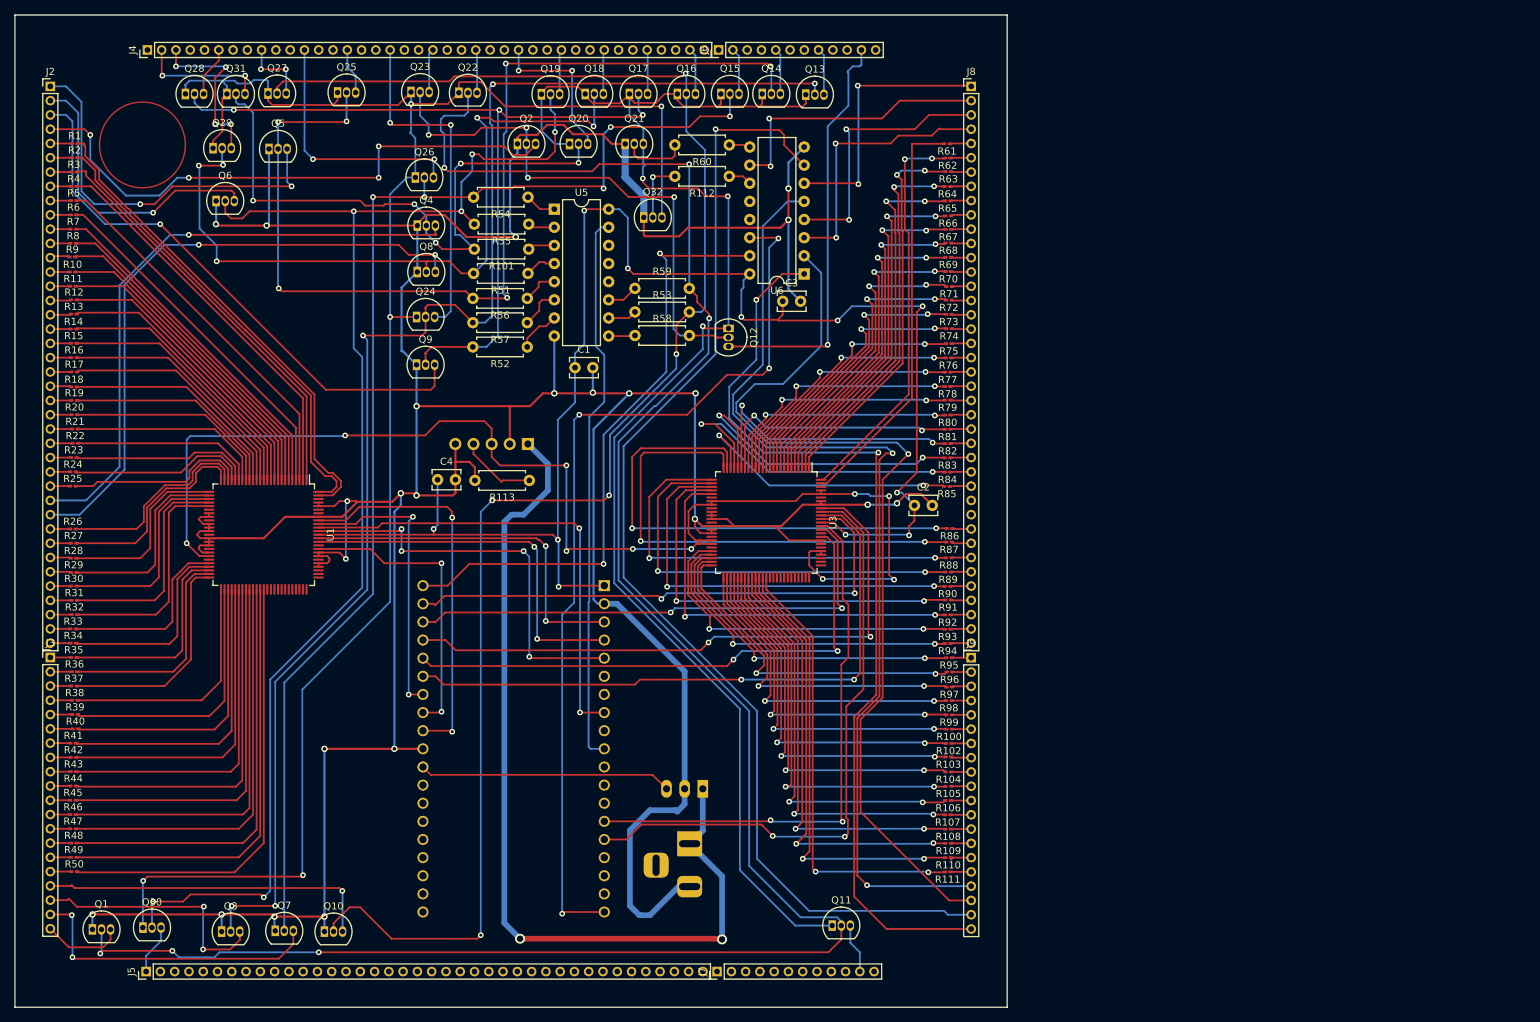
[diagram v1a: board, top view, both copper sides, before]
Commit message: mounting holes added and minor pcb changes
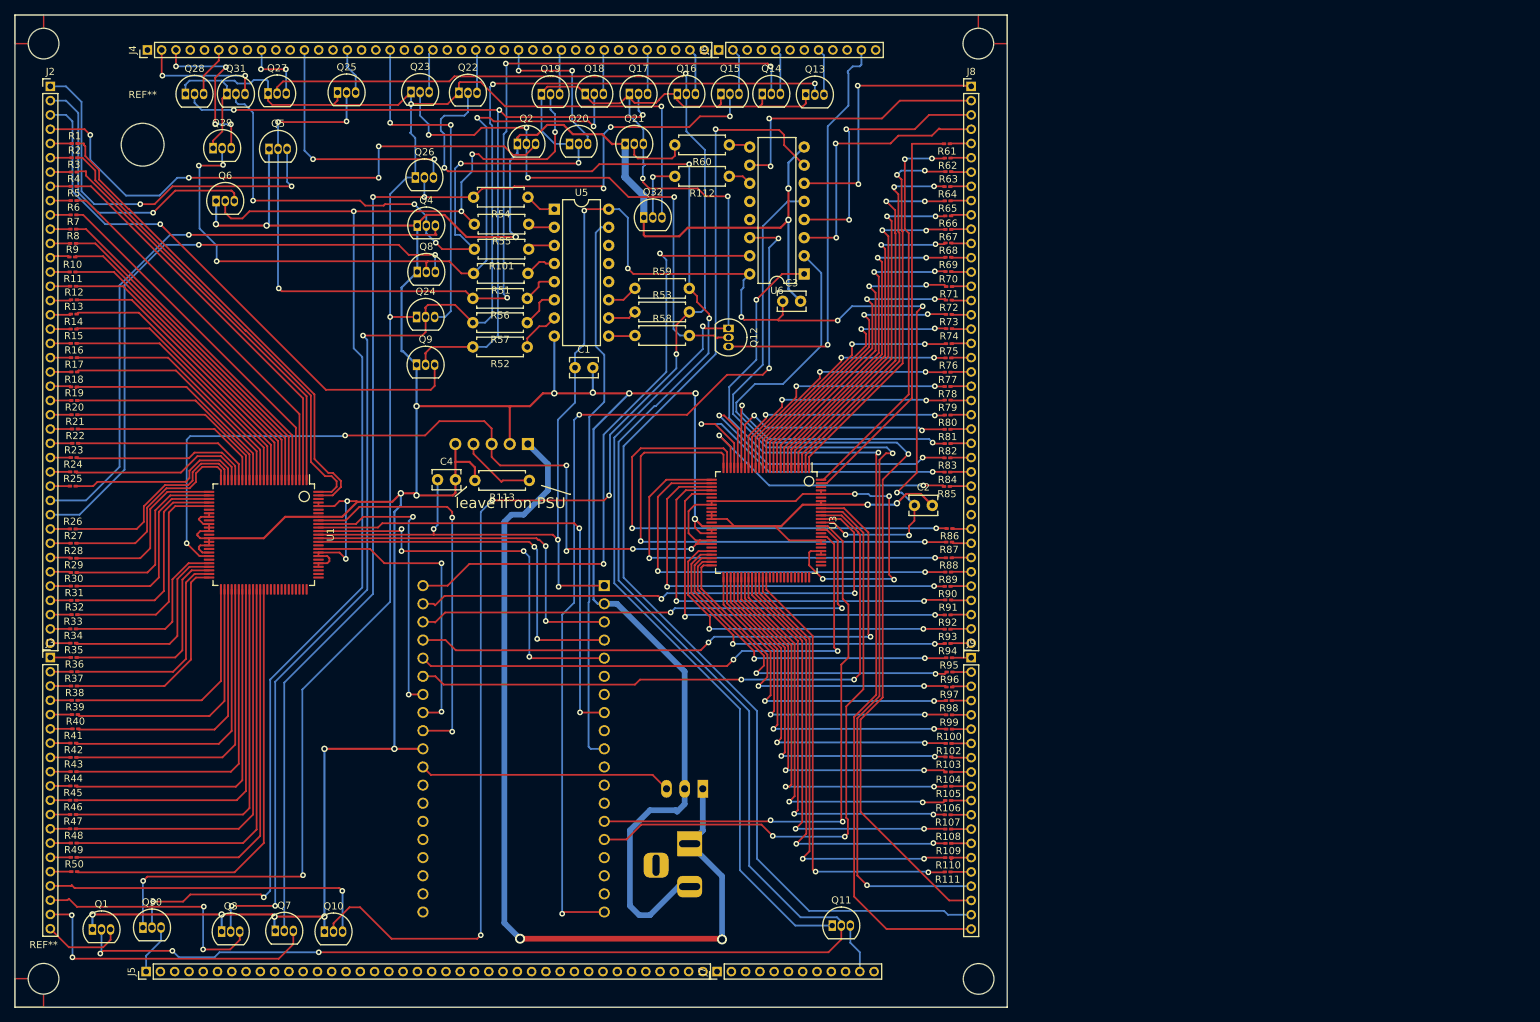
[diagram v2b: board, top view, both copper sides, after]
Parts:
- added ?: , , F.Cu at (221.3, 27.2)
- added ?: , , F.Cu at (221.3, 158.2)
- added ?: , , F.Cu at (90.4, 27.2)
- added REF**: MountingHole_6mm, MountingHole:MountingHole_6mm, F.Cu at (104.2, 41.4)
- added REF**: MountingHole_4.3mm_M4_DIN965, MountingHole:MountingHole_4.3mm_M4_DIN965, F.Cu at (90.3, 158.2)
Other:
- board text added: "leave if on PSU"
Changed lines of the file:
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@@
   (net 436 "Net-(U2-Pad20)")
   (net 437 "Net-(J10-Pad4)")
+  (footprint "" (layer "F.Cu")
+    (at 221.3 27.21)
+    (fp_text reference "" (at 0 0) (layer "F.SilkS")
+      (effects (font (size 1.27 1.27) (thickness 0.15)))
+    )
+    (fp_text value "" (at 0 0) (layer "F.SilkS")
+      (effects (font (size 1.27 1.27) (thickness 0.15)))
+    )
+    (pad "" np_thru_hole circle (at 0 0) (size 4.3 4.3) (drill 4.3) (layers *.Cu *.Mask))
+  )
   (footprint "Resistor_SMD:R_0201_0603Metric_Pad0.64x0.40mm_HandSolder" (layer "F.Cu")
     (at 94.6725 115.2)
@@
     )
   )
+  (footprint "" (layer "F.Cu")
+    (at 221.34 158.23)
+    (fp_text reference "" (at 0 0) (layer "F.SilkS")
+      (effects (font (size 1.27 1.27) (thickness 0.15)))
+    )
+    (fp_text value "" (at 0 0) (layer "F.SilkS")
+      (effects (font (size 1.27 1.27) (thickness 0.15)))
+    )
+    (pad "" np_thru_hole circle (at 0 0) (size 4.3 4.3) (drill 4.3) (layers *.Cu *.Mask))
+  )
   (footprint "Resistor_THT:R_Axial_DIN0207_L6.3mm_D2.5mm_P7.62mm_Horizontal" (layer "F.Cu")
     (at 158.31 56 180)
@@
     )
   )
+  (footprint "MountingHole:MountingHole_6mm" (layer "F.Cu")
+    (at 104.23 41.37)
+    (descr "Mounting Hole 6mm, no annular")
+    (tags "mounting hole 6mm no annular")
+    (attr exclude_from_pos_files exclude_from_bom)
+    (fp_text reference "REF**" (at 0 -7) (layer "F.SilkS")
+      (effects (font (size 1 1) (thickness 0.15)))
+    )
+    (fp_text value "MountingHole_6mm" (at 0 7) (layer "F.Fab")
+      (effects (font (size 1 1) (thickness 0.15)))
+    )
+    (fp_text user "${REFERENCE}" (at 0 0) (layer "F.Fab")
+      (effects (font (size 1 1) (thickness 0.15)))
+    )
+    (fp_circle (center 0 0) (end 6 0) (layer "Cmts.User") (width 0.15) (fill none))
+    (fp_circle (center 0 0) (end 6.25 0) (layer "F.CrtYd") (width 0.05) (fill none))
+    (pad "" np_thru_hole circle (at 0 0) (size 6 6) (drill 6) (layers *.Cu *.Mask))
+  )
   (footprint "Resistor_SMD:R_0201_0603Metric_Pad0.64x0.40mm_HandSolder" (layer "F.Cu")
     (at 217 83.24 180)
@@
     )
   )
+  (footprint "" (layer "F.Cu")
+    (at 90.36 27.21)
+    (fp_text reference "" (at 0 0) (layer "F.SilkS")
+      (effects (font (size 1.27 1.27) (thickness 0.15)))
+    )
+    (fp_text value "" (at 0 0) (layer "F.SilkS")
+      (effects (font (size 1.27 1.27) (thickness 0.15)))
+    )
+    (pad "" np_thru_hole circle (at 0 0) (size 4.3 4.3) (drill 4.3) (layers *.Cu *.Mask))
+  )
   (footprint "Resistor_SMD:R_0201_0603Metric_Pad0.64x0.40mm_HandSolder" (layer "F.Cu")
     (at 217.0675 141.24 180)
@@
     )
   )
+  (footprint "MountingHole:MountingHole_4.3mm_M4_DIN965" (layer "F.Cu")
+    (at 90.35 158.21)
+    (descr "Mounting Hole 4.3mm, no annular, M4, DIN965")
+    (tags "mounting hole 4.3mm no annular m4 din965")
+    (attr exclude_from_pos_files exclude_from_bom)
+    (fp_text reference "REF**" (at 0 -4.75) (layer "F.SilkS")
+      (effects (font (size 1 1) (thickness 0.15)))
+    )
+    (fp_text value "MountingHole_4.3mm_M4_DIN965" (at 0 4.75) (layer "F.Fab")
+      (effects (font (size 1 1) (thickness 0.15)))
+    )
+    (fp_text user "${REFERENCE}" (at 0 0) (layer "F.Fab")
+      (effects (font (size 1 1) (thickness 0.15)))
+    )
+    (fp_circle (center 0 0) (end 3.75 0) (layer "Cmts.User") (width 0.15) (fill none))
+    (fp_circle (center 0 0) (end 4 0) (layer "F.CrtYd") (width 0.05) (fill none))
+    (pad "" np_thru_hole circle (at 0 0) (size 4.3 4.3) (drill 4.3) (layers *.Cu *.Mask))
+  )
   (footprint "Resistor_SMD:R_0201_0603Metric_Pad0.64x0.40mm_HandSolder" (layer "F.Cu")
     (at 217 143.24 180)
@@
     (pad "38" thru_hole circle locked (at 12.7 -25.96 180) (size 1.56 1.56) (drill 1.04) (layers *.Cu *.Mask))
   )
-  (gr_circle (center 104.2 41.4) (end 103.9 47.4) (layer "F.Cu") (width 0.2) (fill none))
+  (gr_rect (start 225.31 23.2) (end 221.3 27.21) (layer "F.Cu") (width 0.2) (fill none))
+  (gr_rect (start 86.35 162.19) (end 90.35 158.19) (layer "F.Cu") (width 0.2) (fill none))
+  (gr_rect (start 86.35 23.2) (end 90.36 27.21) (layer "F.Cu") (width 0.2) (fill none))
+  (gr_line (start 160.1 89.11) (end 164.11 90.36) (layer "F.SilkS") (width 0.15))
+  (gr_line (start 149.51 89.4) (end 149.6 89.24) (layer "F.SilkS") (width 0.15))
+  (gr_circle (center 126.87 90.65) (end 127.13 91.32) (layer "F.SilkS") (width 0.15) (fill none))
+  (gr_line (start 164.11 90.36) (end 164.15 90.3) (layer "F.SilkS") (width 0.15))
+  (gr_circle (center 197.58 88.51) (end 197.04 88.9) (layer "F.SilkS") (width 0.15) (fill none))
+  (gr_line (start 148 90.65) (end 149.51 89.4) (layer "F.SilkS") (width 0.15))
   (gr_rect (start 86.34 23.2) (end 225.34 162.2) (layer "Edge.Cuts") (width 0.1) (fill none))
+  (gr_text "leave if on PSU" (at 155.76 91.57) (layer "F.SilkS")
+    (effects (font (size 1.5 1.5) (thickness 0.3)))
+  )
   (segment (start 98.7 57) (end 94.8875 57) (width 0.25) (layer "F.Cu") (net 1))
   (segment (start 124.2 88.3375) (end 124.2 82.5) (width 0.25) (layer "F.Cu") (net 1))
